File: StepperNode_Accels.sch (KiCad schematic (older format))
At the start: 20 parts

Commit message: First Revision -
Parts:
- removed C? (x12): 100nF, symbol C
- removed R? (x4): 10K, symbol R
- added C12, C13, C14, C15, C16, C17, C18, C19, C20, C21, C22, C23: C_100nF_50V, RLOOP_FOOTPRINTS:rLoop_C_0603, symbol C_100nF_50V
- added R1, R2, R3, R4: 10K, RLOOP_FOOTPRINTS:rLoop_R_0603, symbol 10K
- gave numbers to parts that had none: 4
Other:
- moved on the sheet: U6, U7, U8, U9

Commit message: Update per design review.
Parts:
- added R? (x4): 4.7K, RLOOP_FOOTPRINTS:rLoop_R_0603, symbol 4.7K
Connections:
- wire segments 20 -> 26
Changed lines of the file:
@@
 Title "Accelerometers"
 Date ""
-Rev "1"
+Rev "2"
 Comp ""
 Comment1 ""
@@
 $EndComp
 Wire Wire Line
-	5900 1700 6800 1700
-Wire Wire Line
-	5900 1800 6800 1800
+	5900 1700 7900 1700
+Wire Wire Line
+	5900 1800 7900 1800
 Text Label 6050 1700 0    60   ~ 0
 CHA_I2C_SCL
@@
 $EndComp
 Wire Wire Line
-	5900 4600 6800 4600
-Wire Wire Line
-	5900 4700 6800 4700
+	5900 4600 7850 4600
+Wire Wire Line
+	5900 4700 7850 4700
 Text Label 6050 4600 0    60   ~ 0
 CHB_I2C_SCL
@@
 Text Label 5950 6450 0    60   ~ 0
 CHB_ACCEL2_NINT
-Text HLabel 6800 1700 2    60   Input ~ 0
+Text HLabel 7900 1700 2    60   Input ~ 0
 CHA_I2C_SCL
-Text HLabel 6800 1800 2    60   BiDi ~ 0
+Text HLabel 7900 1800 2    60   BiDi ~ 0
 CHA_I2C_SDA
 Text HLabel 7600 2150 2    60   Output ~ 0
@@
 	0    -1   -1   0
 $EndComp
-Text HLabel 6800 4600 2    60   Input ~ 0
+Text HLabel 7850 4600 2    60   Input ~ 0
 CHB_I2C_SCL
-Text HLabel 6800 4700 2    60   BiDi ~ 0
+Text HLabel 7850 4700 2    60   BiDi ~ 0
 CHB_I2C_SDA
 $Comp
@@
 	1    0    0    -1
 $EndComp
+$Comp
+L 4.7K R?
+U 1 1 575CC544
+P 6950 1350
+F 0 "R?" V 7030 1350 50  0000 C CNN
+F 1 "4.7K" V 6950 1350 50  0000 C CNN
+F 2 "RLOOP_FOOTPRINTS:rLoop_R_0603" V 6880 1350 50  0001 C CNN
+F 3 "" H 6950 1350 50  0000 C CNN
+	1    6950 1350
+	1    0    0    -1
+$EndComp
+$Comp
+L 4.7K R?
+U 1 1 575CC5B1
+P 7200 1350
+F 0 "R?" V 7280 1350 50  0000 C CNN
+F 1 "4.7K" V 7200 1350 50  0000 C CNN
+F 2 "RLOOP_FOOTPRINTS:rLoop_R_0603" V 7130 1350 50  0001 C CNN
+F 3 "" H 7200 1350 50  0000 C CNN
+	1    7200 1350
+	1    0    0    -1
+$EndComp
+$Comp
+L +3V3_A #PWR?
+U 1 1 575CC5CD
+P 6950 1200
+F 0 "#PWR?" H 6950 1050 50  0001 C CNN
+F 1 "+3V3_A" H 6950 1340 50  0000 C CNN
+F 2 "" H 6950 1200 60  0000 C CNN
+F 3 "" H 6950 1200 60  0000 C CNN
+	1    6950 1200
+	1    0    0    -1
+$EndComp
+Wire Wire Line
+	6950 1200 7200 1200
+Wire Wire Line
+	6950 1500 6950 1700
+Connection ~ 6950 1700
+Wire Wire Line
+	7200 1500 7200 1800
+Connection ~ 7200 1800
+$Comp
+L 4.7K R?
+U 1 1 575CC8DB
+P 7250 4250
+F 0 "R?" V 7330 4250 50  0000 C CNN
+F 1 "4.7K" V 7250 4250 50  0000 C CNN
+F 2 "RLOOP_FOOTPRINTS:rLoop_R_0603" V 7180 4250 50  0001 C CNN
+F 3 "" H 7250 4250 50  0000 C CNN
+	1    7250 4250
+	1    0    0    -1
+$EndComp
+$Comp
+L 4.7K R?
+U 1 1 575CC8E1
+P 7500 4250
+F 0 "R?" V 7580 4250 50  0000 C CNN
+F 1 "4.7K" V 7500 4250 50  0000 C CNN
+F 2 "RLOOP_FOOTPRINTS:rLoop_R_0603" V 7430 4250 50  0001 C CNN
+F 3 "" H 7500 4250 50  0000 C CNN
+	1    7500 4250
+	1    0    0    -1
+$EndComp
+Wire Wire Line
+	7250 4100 7500 4100
+Wire Wire Line
+	7250 4400 7250 4600
+Connection ~ 7250 4600
+Wire Wire Line
+	7500 4400 7500 4700
+Connection ~ 7500 4700
+$Comp
+L +3V3_B #PWR?
+U 1 1 575CCA5D
+P 7250 4100
+F 0 "#PWR?" H 7250 3950 50  0001 C CNN
+F 1 "+3V3_B" H 7250 4240 50  0000 C CNN
+F 2 "" H 7250 4100 60  0000 C CNN
+F 3 "" H 7250 4100 60  0000 C CNN
+	1    7250 4100
+	1    0    0    -1
+$EndComp

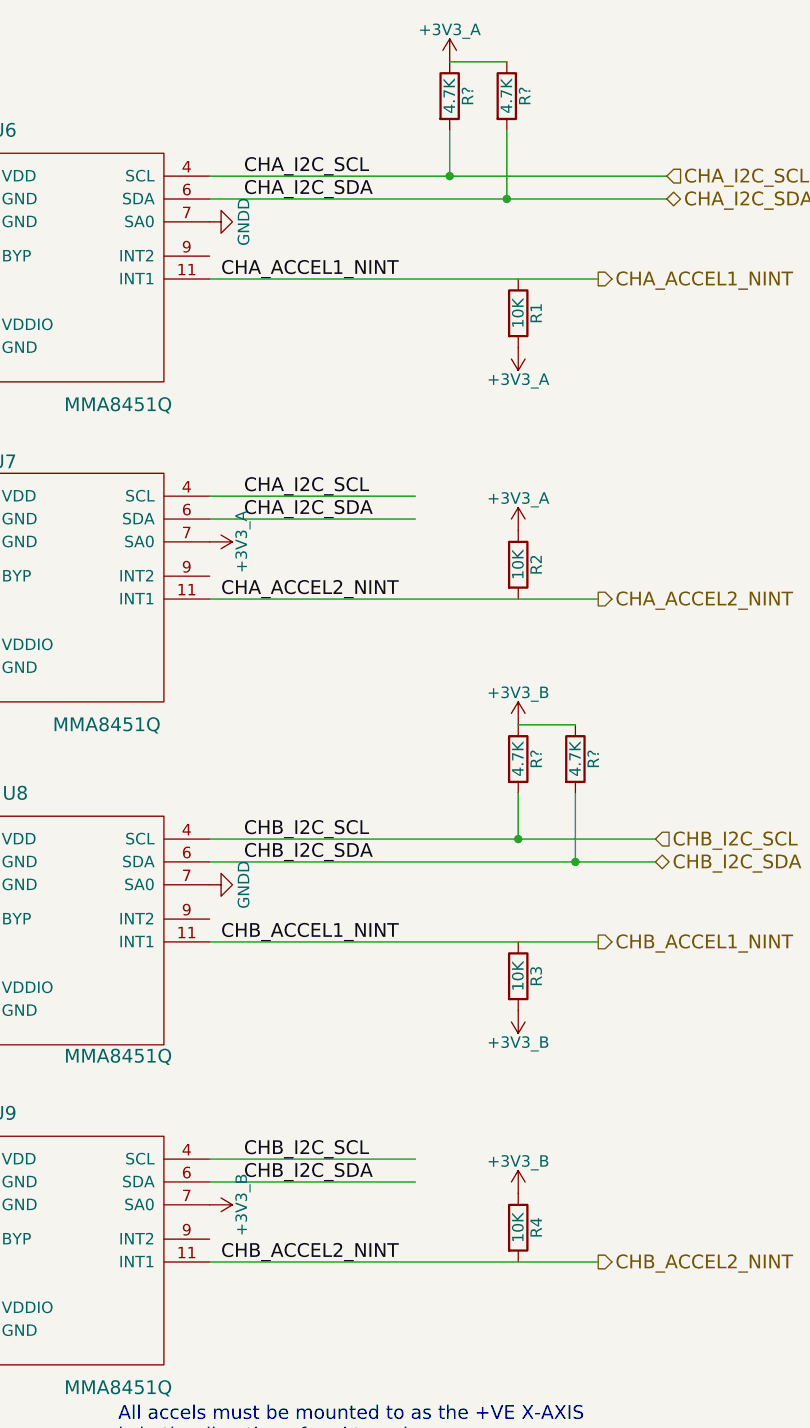
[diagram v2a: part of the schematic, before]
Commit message: Fix most ERC warnings (non-connected pins, etc)
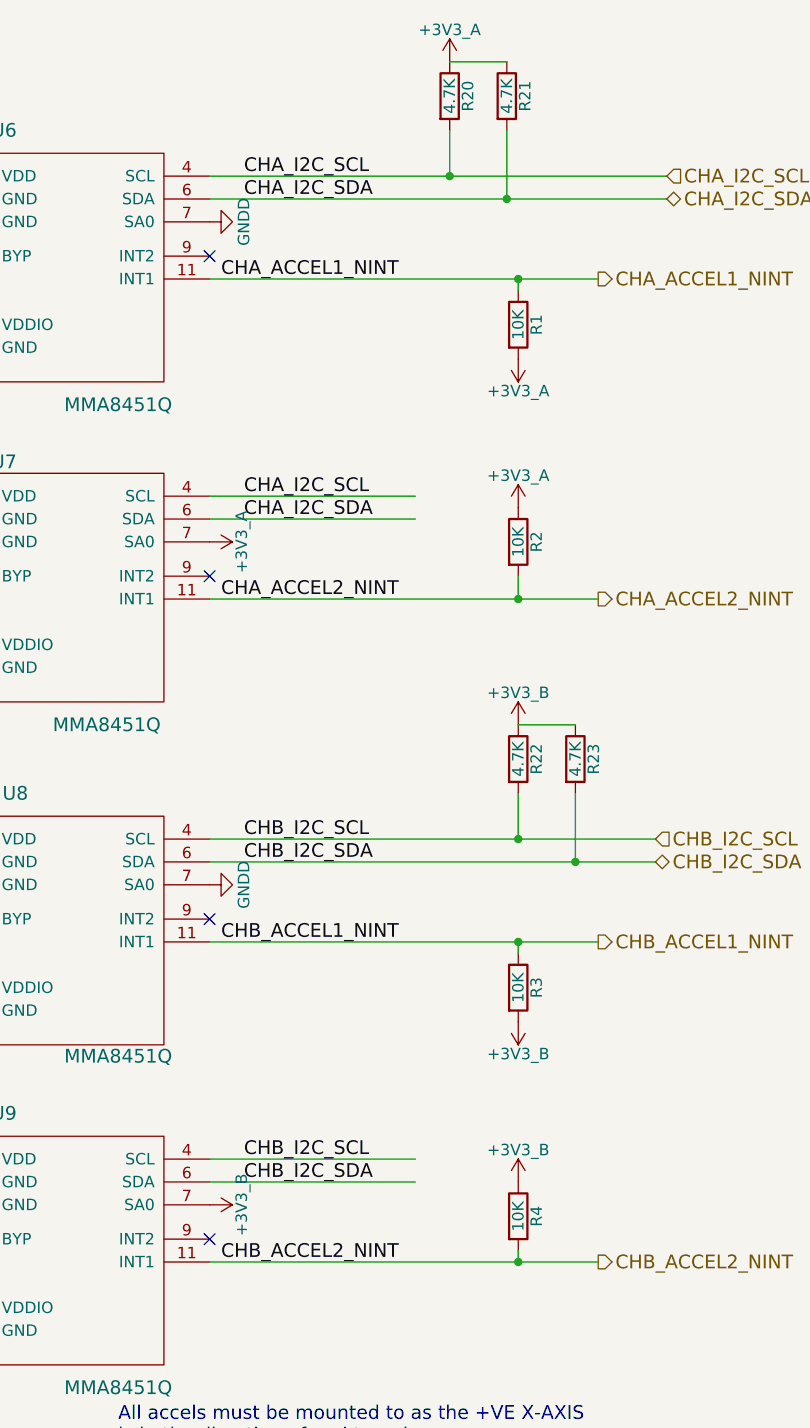
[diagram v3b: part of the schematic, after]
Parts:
- gave numbers to parts that had none: 4
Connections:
- wire segments 26 -> 30
- no-connect marks 0 -> 4
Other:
- moved on the sheet: R1, R2, R3, R4
